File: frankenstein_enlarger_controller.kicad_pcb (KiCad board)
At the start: 4 copper layers, 174.8 x 120.2 mm, 172 parts, among them J1 Screw_Terminal_01x04, SW1 RotaryEncoder_Switch, SW2 RotaryEncoder_Switch, SW3 RotaryEncoder_Switch, SW4 RotaryEncoder_Switch, SW5 E-SWITCH 5501M, SW6 E-SWITCH 5501M, SW7 E-SWITCH 5501M, SW8 E-SWITCH 5501M, U1 74HC595, U10 74HC595, U11 74HC595, U12 74HC595, U2 74HC595, U26 74HC595, U27 SP3485EN-L/TR, U3 74HC595, U4 74HC595, U5 74HC595, U6 74HC595, U7 74HC595, U8 74HC595, U9 74HC595

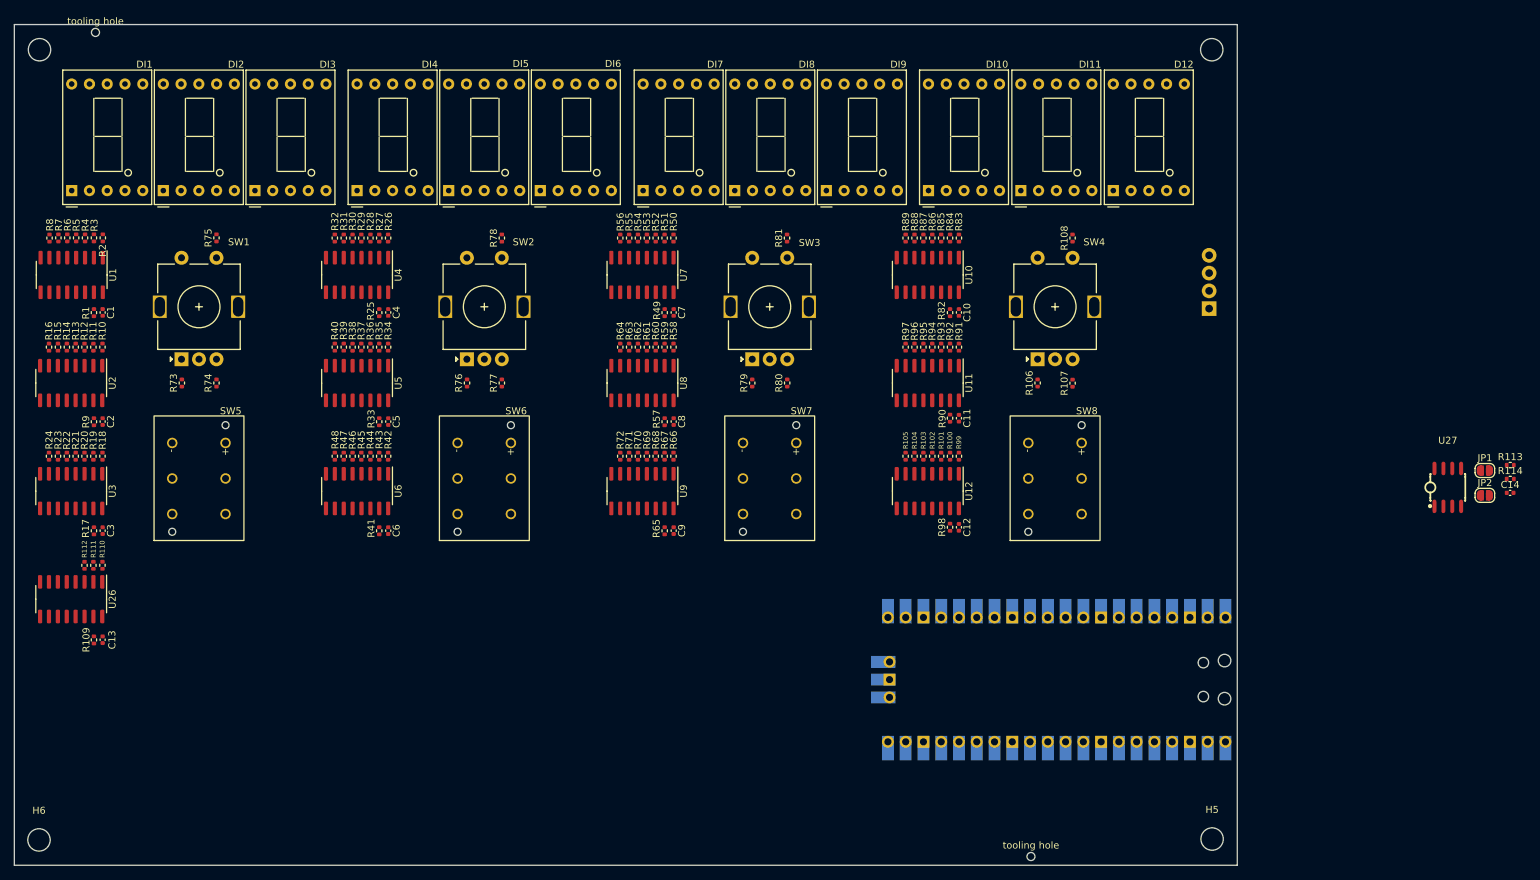
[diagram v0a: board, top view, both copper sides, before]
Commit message: First maybe complete version?
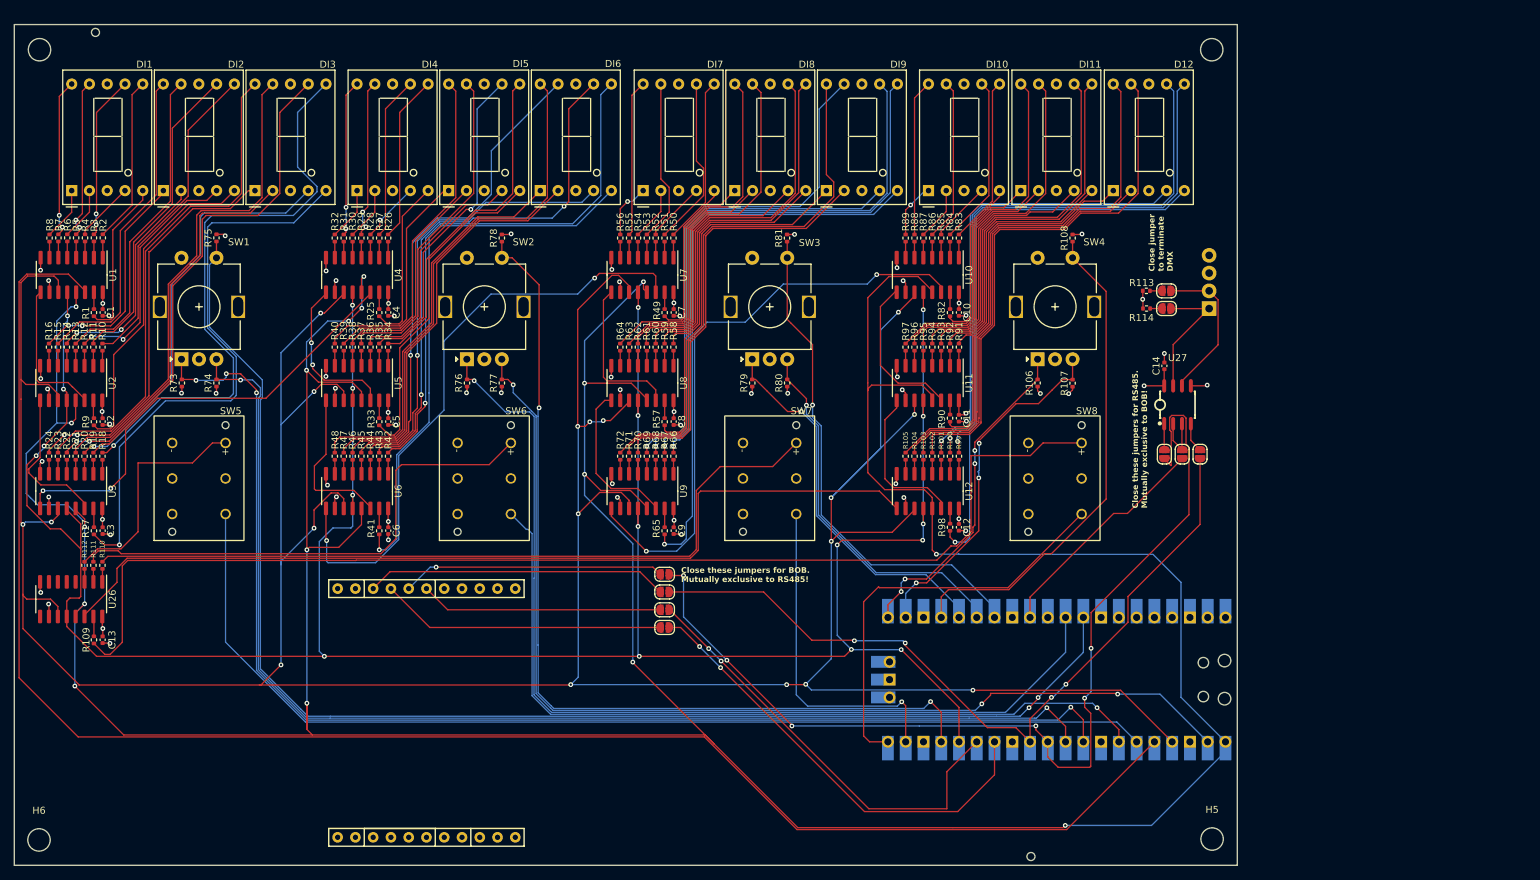
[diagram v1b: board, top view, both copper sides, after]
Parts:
- added JP3: DMX_ENABLE_RX, Jumper:SolderJumper-2_P1.3mm_Open_RoundedPad1.0x1.5mm, F.Cu at (178.7, 75.4)
- added JP4: BOB_ENABLE_SDI, Jumper:SolderJumper-2_P1.3mm_Open_RoundedPad1.0x1.5mm, F.Cu at (107.3, 92.6)
- added JP5: DMX_ENABLE_TX, Jumper:SolderJumper-2_P1.3mm_Open_RoundedPad1.0x1.5mm, F.Cu at (183.8, 75.4)
- added JP6: BOB_ENABLE_CSN, Jumper:SolderJumper-2_P1.3mm_Open_RoundedPad1.0x1.5mm, F.Cu at (107.3, 95.1)
- added JP7: DMX_ENABLE_EN, Jumper:SolderJumper-2_P1.3mm_Open_RoundedPad1.0x1.5mm, F.Cu at (181.3, 75.4)
- added JP8: BOB_ENABLE_SDO, Jumper:SolderJumper-2_P1.3mm_Open_RoundedPad1.0x1.5mm, F.Cu at (107.3, 97.7)
- added JP9: BOB_ENABLE_SCK, Jumper:SolderJumper-2_P1.3mm_Open_RoundedPad1.0x1.5mm, F.Cu at (107.3, 100.2)
- added U13: ~, BOB:BOB5160, B.Cu at (59.1, 93.3)
- moved R113 57.7 mm to (176.2, 52.1), turned to 180 degrees
- moved R114 57.4 mm to (176.2, 54.6)
- moved JP2 52.8 mm to (179.0, 54.6), turned to 180 degrees
- moved C14 52.7 mm to (178.7, 62.8), turned to 90 degrees
- moved JP1 52.3 mm to (179.0, 52.1)
- moved U27 40.4 mm to (180.6, 68.4)
- turned R90 to -90 degrees
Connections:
- U27 pad 1: /UART0_RX -> /RS485/RS485_RX
- U27 pad 2: /UART0_EN -> /RS485/RS485_EN
- U27 pad 3: /UART0_EN -> /RS485/RS485_EN
- U27 pad 4: /UART0_TX -> /RS485/RS485_TX
- UP1 pad 1: /UART0_TX -> PWM
- UP1 pad 11: /SW1_S -> /UART1_TX_SPI1_RX
- UP1 pad 12: /SW2_A -> /UART1_RX_SPI1_CSN
- UP1 pad 14: /SW2_B -> /SPI1_CLK
- UP1 pad 15: PWM -> /SPI1_TX
- UP1 pad 2: /UART0_RX -> /SW2_B
- UP1 pad 31: unconnected-(UP1-GPIO26_ADC0-Pad31) -> /SW2_A
- UP1 pad 32: unconnected-(UP1-GPIO27_ADC1-Pad32) -> /SW1_S
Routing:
- net PWM: track 0.00 -> 584.0 mm, vias 0 -> 17
- net SPI0_SCK: track 0.00 -> 520.2 mm, vias 0 -> 18
- net LATCH: track 0.00 -> 385.7 mm, vias 0 -> 19
- net /SPIO_TX: track 0.00 -> 244.2 mm
- net /SW1_S: track 0.00 -> 194.1 mm, vias 0 -> 2
- net /SW1_A: track 0.00 -> 181.3 mm, vias 0 -> 4
- net /SW1_B: track 0.00 -> 172.3 mm, vias 0 -> 2
- net Net-(R109-Pad2): track 0.00 -> 167.2 mm
- net /SW5: track 0.00 -> 154.5 mm
- net /SW2_B: track 0.00 -> 151.4 mm, vias 0 -> 3
- net /UART1_TX_SPI1_RX: track 0.00 -> 144.4 mm, vias 0 -> 6
- net /SW2_A: track 0.00 -> 140.1 mm, vias 0 -> 1
- net /SW2_S: track 0.00 -> 131.5 mm, vias 0 -> 2
- net /Digit12/DATA_OUT: track 0.00 -> 130.7 mm
- net /SW6: track 0.00 -> 116.3 mm, vias 0 -> 1
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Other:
- board text added: "Close jumper to terminate DMX"
- board text added: "Close these jumpers for BOB. Mutually exclusive to RS485!"
- board text added: "Close these jumpers for RS485. Mutually exclusive to BOB!"

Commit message: Implemented fixes/changes after @manawyrm review
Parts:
- removed D12: D168K, Display_7Segment:D1X8K
- removed JP2: DMX+Termination, Jumper:SolderJumper-2_P1.3mm_Open_RoundedPad1.0x1.5mm
- removed R114: 120, Resistor_SMD:R_0402_1005Metric
- added DI12: D168K, Display_7Segment:D1X8K, F.Cu at (171.4, 37.7)
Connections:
- R113 pad 2: GND -> /RS485/DMX+
- SW5 pad 2: /SW5 -> unconnected-(SW5-C-Pad2)
- SW5 pad 3: unconnected-(SW5-C-Pad3) -> /SW5
- SW6 pad 2: /SW6 -> unconnected-(SW6-C-Pad2)
- SW6 pad 3: unconnected-(SW6-C-Pad3) -> /SW6
- SW7 pad 2: /SW7 -> unconnected-(SW7-C-Pad2)
- SW7 pad 3: unconnected-(SW7-C-Pad3) -> /SW7
- SW8 pad 2: /SW8 -> unconnected-(SW8-C-Pad2)
- SW8 pad 3: unconnected-(SW8-C-Pad3) -> /SW8
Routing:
- net /SW6: track 116.3 -> 124.0 mm
- net /SW7: track 47.8 -> 53.7 mm
- net /RS485/DMX+: track 18.6 -> 24.3 mm
- net /SW5: track 154.5 -> 159.2 mm
- net /SW8: track 59.5 -> 54.8 mm
- net GND: track 41.1 -> 38.6 mm, vias 29 -> 28
- net Net-(JP2-B): track 1.69 -> 0.00 mm

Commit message: Various stuff I've forgotten to commit
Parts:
- added REF**: frankenlogo, frankenlogo:frankenlogo, F.Cu at (29.9, 128.1)
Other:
- board text added: "Frankenstein Lab Controller wirkbetrieb.net / Tom Eichhorn Rev A1"
- board text added: "JLCJLCJLCJLC"

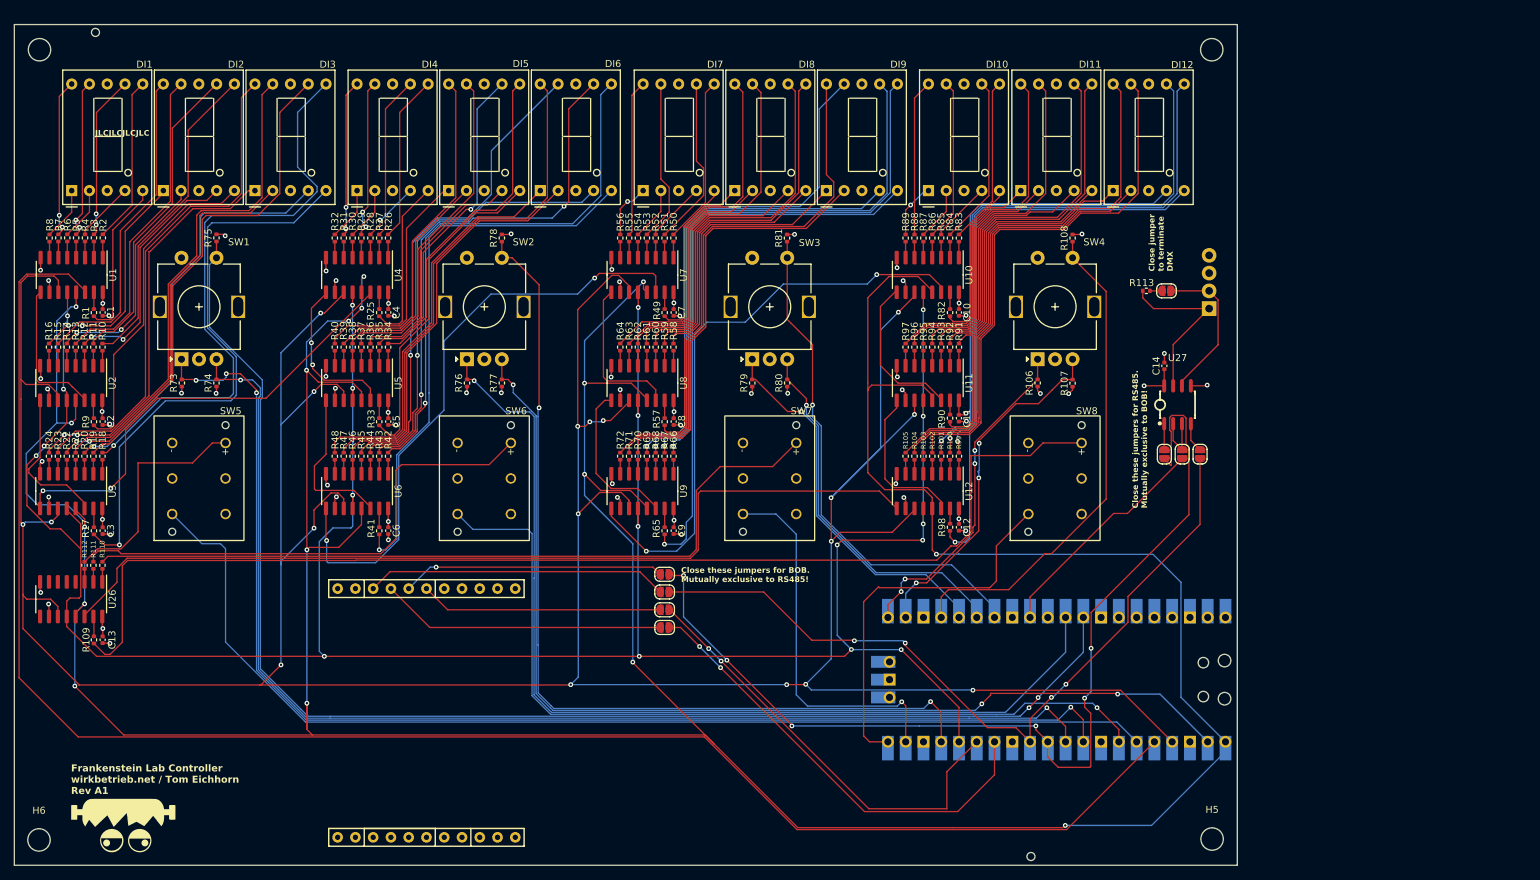
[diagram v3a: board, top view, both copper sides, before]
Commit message: Consolidated Hardware on single board
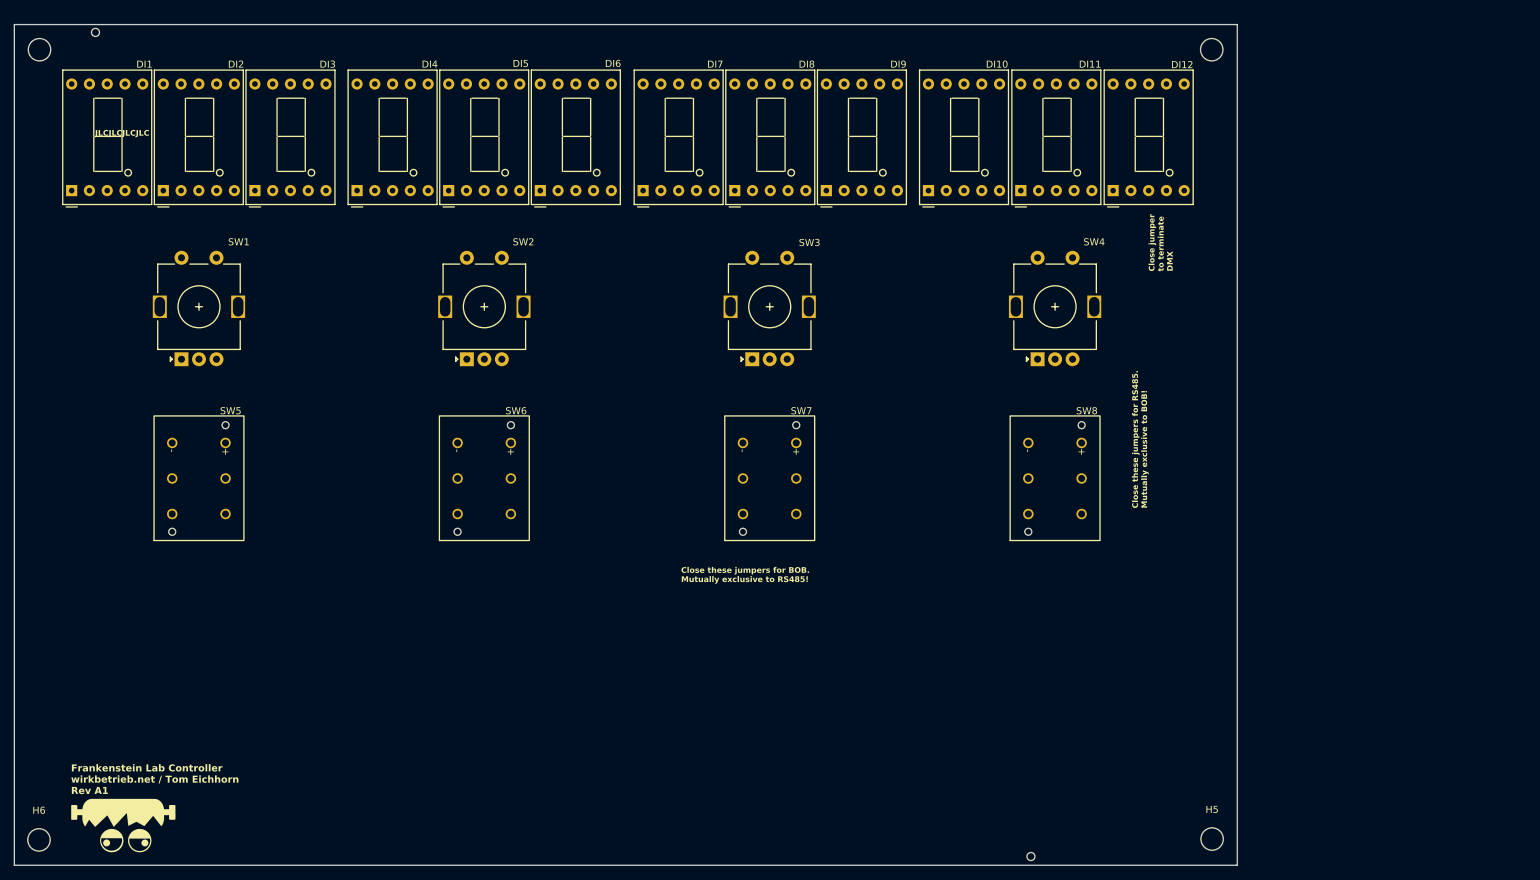
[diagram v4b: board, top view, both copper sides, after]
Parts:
- removed C1, C10, C11, C12, C13, C14, C2, C3, C4, C5, C6, C7, C8, C9: 100n, Capacitor_SMD:C_0402_1005Metric
- removed J1: Screw_Terminal_01x04, TerminalBlock_TE-Connectivity:TerminalBlock_TE_282834-4_1x04_P2.54mm_Horizontal
- removed JP1: DMX-Termination, Jumper:SolderJumper-2_P1.3mm_Open_RoundedPad1.0x1.5mm
- removed JP3: DMX_ENABLE_RX, Jumper:SolderJumper-2_P1.3mm_Open_RoundedPad1.0x1.5mm
- removed JP4: BOB_ENABLE_SDI, Jumper:SolderJumper-2_P1.3mm_Open_RoundedPad1.0x1.5mm
- removed JP5: DMX_ENABLE_TX, Jumper:SolderJumper-2_P1.3mm_Open_RoundedPad1.0x1.5mm
- removed JP6: BOB_ENABLE_CSN, Jumper:SolderJumper-2_P1.3mm_Open_RoundedPad1.0x1.5mm
- removed JP7: DMX_ENABLE_EN, Jumper:SolderJumper-2_P1.3mm_Open_RoundedPad1.0x1.5mm
- removed JP8: BOB_ENABLE_SDO, Jumper:SolderJumper-2_P1.3mm_Open_RoundedPad1.0x1.5mm
- removed JP9: BOB_ENABLE_SCK, Jumper:SolderJumper-2_P1.3mm_Open_RoundedPad1.0x1.5mm
- removed R1, R10, R100, R101, R102, R103, R104, R105, R109, R11, R110, R111, R112, R113, R12, R13, R14, R15, R16, R17, R18, R19, R2, R20, R21, R22, R23, R24, R25, R26, R27, R28, R29, R3, R30, R31, R32, R33, R34, R35, R36, R37, R38, R39, R4, R40, R41, R42, R43, R44, R45, R46, R47, R48, R49, R5, R50, R51, R52, R53, R54, R55, R56, R57, R58, R59, R6, R60, R61, R62, R63, R64, R65, R66, R67, R68, R69, R7, R70, R71, R72, R8, R82, R83, R84, R85, R86, R87, R88, R89, R9, R90, R91, R92, R93, R94, R95, R96, R97, R98, R99: 120, Resistor_SMD:R_0402_1005Metric
- removed R106, R107, R108, R73, R74, R75, R76, R77, R78, R79, R80, R81: 5.1k, Resistor_SMD:R_0402_1005Metric
- removed U1, U10, U11, U12, U2, U26, U3, U4, U5, U6, U7, U8, U9: 74HC595, Package_SO:SOIC-16_3.9x9.9mm_P1.27mm
- removed U13: ~, BOB:BOB5160
- removed U27: SP3485EN-L/TR, easyeda2kicad:SOIC-8_L5.0-W4.0-P1.27-LS6.0-BL
- removed UP1: Pico, MCU_RaspberryPi_and_Boards:RPi_Pico_SMD_TH
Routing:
- net PWM: track 584.0 -> 0.00 mm, vias 17 -> 0
- net SPI0_SCK: track 520.2 -> 0.00 mm, vias 18 -> 0
- net LATCH: track 385.7 -> 0.00 mm, vias 19 -> 0
- net /SPIO_TX: track 244.2 -> 0.00 mm
- net /SW1_S: track 194.1 -> 0.00 mm, vias 2 -> 0
- net /SW1_A: track 181.3 -> 0.00 mm, vias 4 -> 0
- net /SW1_B: track 172.3 -> 0.00 mm, vias 2 -> 0
- net Net-(R109-Pad2): track 167.2 -> 0.00 mm
- net /SW5: track 159.2 -> 0.00 mm
- net /SW2_B: track 151.4 -> 0.00 mm, vias 3 -> 0
- net /UART1_TX_SPI1_RX: track 144.4 -> 0.00 mm, vias 6 -> 0
- net /SW2_A: track 140.1 -> 0.00 mm, vias 1 -> 0
- net /SW2_S: track 131.5 -> 0.00 mm, vias 2 -> 0
- net /Digit12/DATA_OUT: track 130.7 -> 0.00 mm
- net /SW6: track 124.0 -> 0.00 mm, vias 1 -> 0
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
